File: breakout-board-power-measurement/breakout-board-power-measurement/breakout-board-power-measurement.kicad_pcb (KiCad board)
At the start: 2 copper layers, 62 parts, among them J1 Screw_Terminal_01x04, J2 Conn_01x07, J3 Conn_01x07, J4 Conn_01x02, Q1 NMOS, Q2 NMOS, U1 MCP3911A0-E-SS, U2 Si8641BA-B-IU, U3 LM317_3PinPackage, U4 LM2575-3.3BT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

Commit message: Important updates and fine tunings to schematic
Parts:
- removed D1, D2: 3.6, Diode_SMD:D_1206_3216Metric
- removed PS1: ITQ4803SA-H, Converter_DCDC:Converter_DCDC_XP_POWER-ITQxxxxS-H_THT
- removed Q1, Q2: NMOS, Package_TO_SOT_SMD:TO-252-2
- removed U4: LM2575-3.3BT, Package_TO_SOT_THT:TO-220-5_Vertical
- added PS2: IA0505S, Converter_DCDC:Converter_DCDC_XP_POWER-IAxxxxS_THT, F.Cu at (154.1, 90.9)
- J2: value Conn_01x07 -> Conn_01x09; footprint Connector_PinSocket_2.54mm:PinSocket_1x07_P2.54mm_Vertical -> Connector_PinSocket_2.54mm:PinSocket_1x09_P2.54mm_Vertical
- R10, R11: value 10k -> 180k
- R6, R7: value 270k -> 150k
- R8: value 100k -> 10k
- R9: value 10E -> 50m
- U2: footprint Package_SO:QSOP-16_3.9x4.9mm_P0.635mm -> Package_SO:SOIC-16_3.9x9.9mm_P1.27mm
- U3: value LM317_3PinPackage -> LM317_TO-252; footprint Package_TO_SOT_SMD:SOT-89-3_Handsoldering -> Package_TO_SOT_SMD:TO-252-2
- moved U3 59.0 mm to (169.9, 111.4)
- moved R10 39.2 mm to (167.0, 82.0), turned to 0 degrees
- moved R11 36.6 mm to (167.0, 85.3)
- moved C10 11.6 mm to (176.5, 121.8)
- moved C9 11.6 mm to (160.7, 121.8)
- moved FB1 11.6 mm to (168.5, 121.8)
- moved R13 11.6 mm to (167.1, 126.9)
- moved R14 11.6 mm to (170.4, 126.9)
- moved C11 1.98 mm to (205.1, 134.8)
- moved C12 1.98 mm to (205.1, 138.2)
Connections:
- R10 pad 1: Net-(D1-A) -> Net-(R10-Pad1)
- R10 pad 2: GNDA -> Net-(R10-Pad2)
- R11 pad 1: Net-(D2-A) -> Net-(R10-Pad2)
- R11 pad 2: GNDD -> Net-(R11-Pad2)
- R7 pad 2: Net-(R7-Pad2) -> Net-(R10-Pad1)
- R8 pad 1: Net-(R7-Pad2) -> Net-(R11-Pad2)
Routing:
- net Net-(R7-Pad2): track 27.8 -> 0.00 mm
- net (no net): track 0.00 -> 27.8 mm

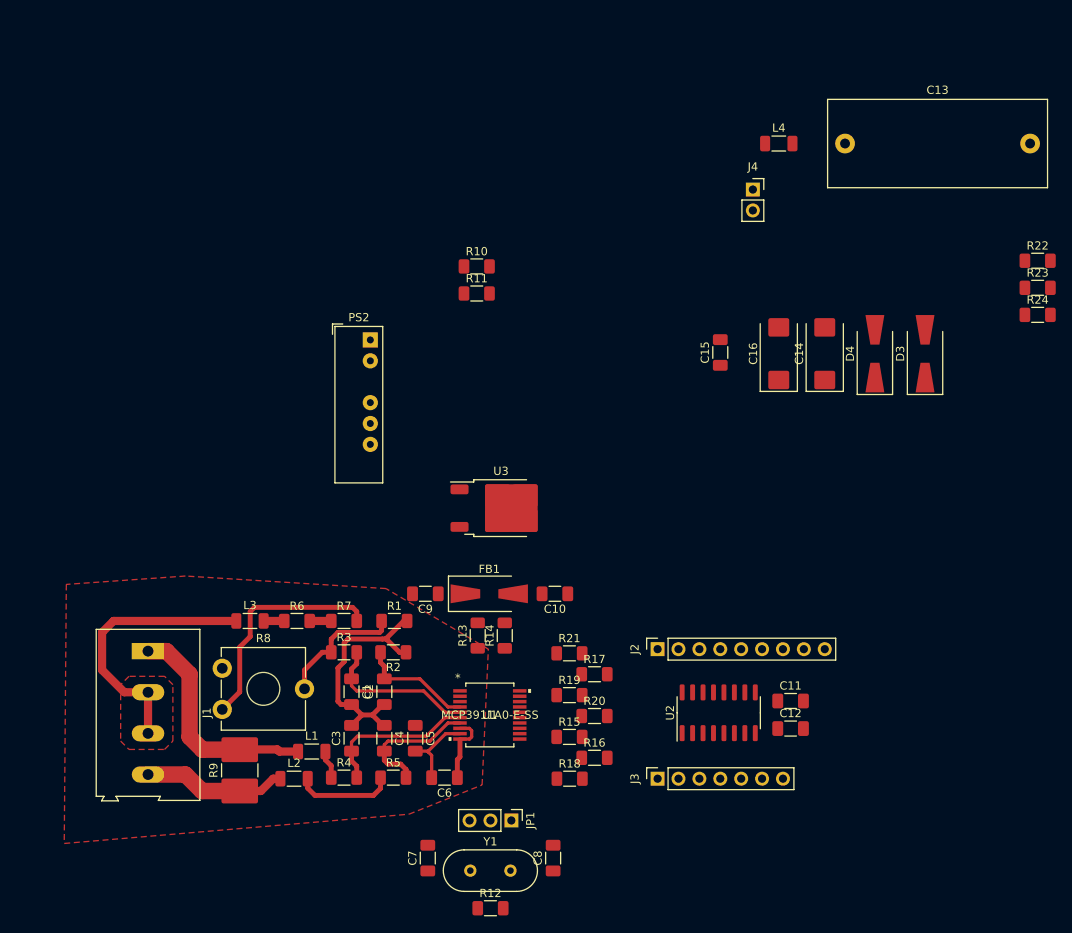
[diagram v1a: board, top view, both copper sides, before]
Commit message: Power measurement PCB 95% Done. Whats missing: proper cooil footprints, capacitive power supply net
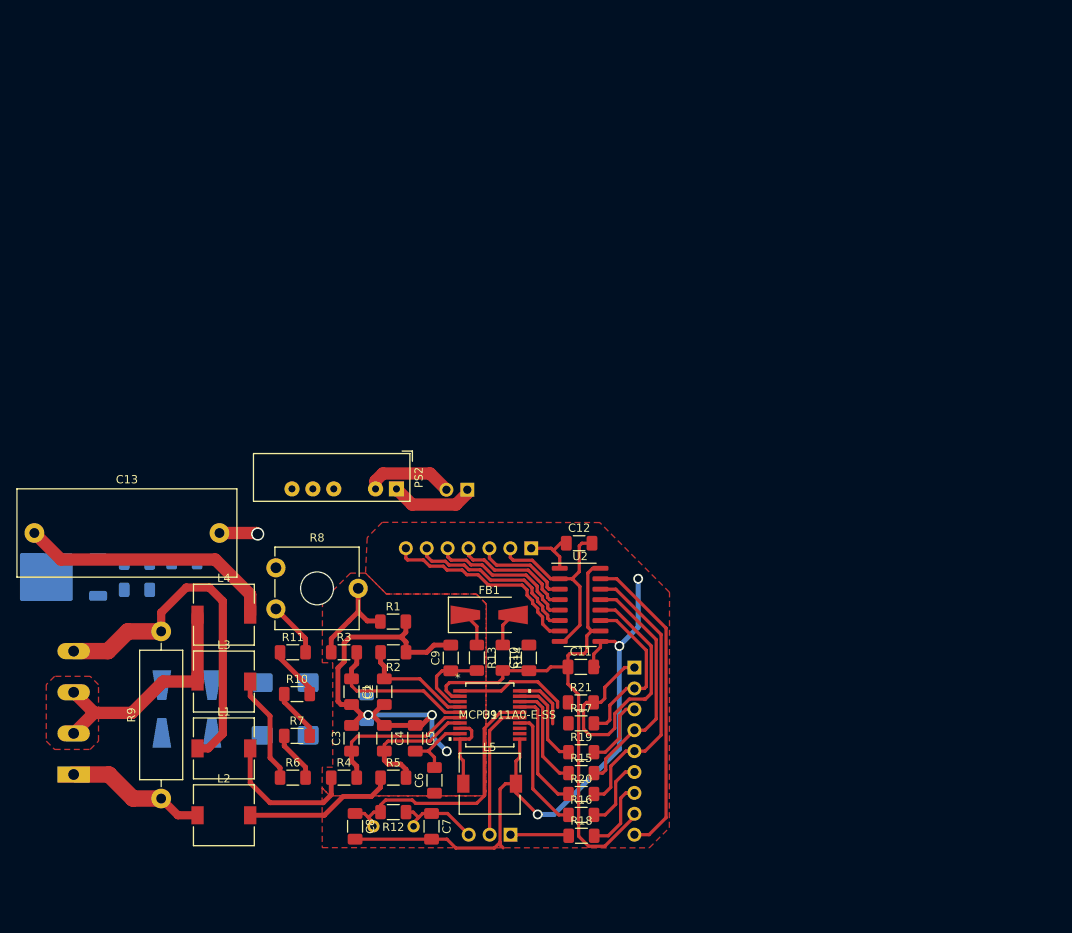
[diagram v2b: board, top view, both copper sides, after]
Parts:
- added L5: 150n/300m, Inductor_SMD:L_7.3x7.3_H4.5, F.Cu at (168.6, 144.9)
- C14, C15, C16, D3, D4, J1, J2, J3, J4, JP1, R22, R23, R24, U3, Y1: moved to B.Cu
- L1, L2, L3, L4: footprint Inductor_SMD:L_1206_3216Metric_Pad1.22x1.90mm_HandSolder -> Inductor_SMD:L_7.3x7.3_H4.5
- R9: footprint Resistor_SMD:R_2816_7142Metric -> Resistor_THT:R_Axial_DIN0516_L15.5mm_D5.0mm_P20.32mm_Horizontal
- moved R23 114.5 mm to (125.7, 118.0), turned to 180 degrees
- moved R24 114.5 mm to (125.7, 121.3), turned to 180 degrees
- moved R22 110.0 mm to (131.4, 118.0), turned to 180 degrees
- moved C13 109.3 mm to (113.2, 114.4)
- moved D3 102.3 mm to (128.7, 135.8)
- moved D4 91.4 mm to (134.8, 135.8)
- moved L4 88.5 mm to (136.2, 124.3)
- moved C14 80.9 mm to (140.9, 135.8)
- moved C16 71.7 mm to (146.5, 135.8)
- moved C15 60.9 mm to (153.6, 135.6)
- moved R10 56.4 mm to (145.1, 134.0)
- moved U3 54.7 mm to (115.9, 119.8), turned to 180 degrees
- moved J4 50.4 mm to (165.8, 109.1), turned to 90 degrees
- moved R11 49.0 mm to (144.6, 128.9)
- moved C12 34.2 mm to (179.4, 115.6)
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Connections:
- C12 pad 2: Net-(J3-Pin_7) -> Net-(J3-Pin_2)
- J1 pad 1: /current_pos -> /current_neg
- J1 pad 2: /HIGH_in -> HIGH_in
- J1 pad 3: /HIGH_in -> HIGH_in
- J1 pad 4: /current_neg -> /current_pos
- L3 pad 1: /HIGH_in -> HIGH_in
- L4 pad 1: HIGH -> HIGH_in
- R15 pad 2: Net-(J2-Pin_3) -> Net-(J2-Pin_4)
- R18 pad 2: Net-(J2-Pin_5) -> Net-(J2-Pin_7)
- R19 pad 2: Net-(J2-Pin_1) -> Net-(J2-Pin_3)
- R20 pad 2: Net-(J2-Pin_4) -> Net-(J2-Pin_5)
- R21 pad 2: Net-(J2-Pin_7) -> Net-(J2-Pin_1)
- U2 pad 13: Net-(J2-Pin_3) -> Net-(J2-Pin_4)
- U2 pad 14: Net-(J2-Pin_4) -> Net-(J2-Pin_5)
- U2 pad 2: Net-(J3-Pin_7) -> Net-(J3-Pin_2)
- U2 pad 7: Net-(J3-Pin_2) -> Net-(J3-Pin_7)
- U2 pad 8: Net-(J3-Pin_7) -> Net-(J3-Pin_2)
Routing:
- net GNDD: track 0.00 -> 117.9 mm, vias 0 -> 3
- net /3V3D: track 0.00 -> 65.8 mm
- net Net-(J2-Pin_1): track 0.00 -> 37.2 mm
- net Net-(J2-Pin_5): track 0.00 -> 34.5 mm
- net /HIGH_in: track 33.2 -> 0.00 mm
- net /OSC2: track 0.00 -> 32.5 mm
- net Net-(C13-Pad1): track 0.00 -> 31.8 mm
- net Net-(J2-Pin_4): track 0.00 -> 29.5 mm
- net HIGH_in: track 0.00 -> 29.3 mm
- net (no net): track 27.8 -> 0.00 mm
- net GNDA: track 38.5 -> 64.0 mm, vias 0 -> 3
- net Net-(J3-Pin_2): track 0.00 -> 25.0 mm
- net Net-(J3-Pin_7): track 0.00 -> 24.9 mm
- net Net-(J3-Pin_6): track 0.00 -> 21.4 mm
- net Net-(J2-Pin_2): track 0.00 -> 20.7 mm
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- added copper zone on F.Cu, net GNDD
- added copper zone on F.Cu, net HIGH_in
- removed copper zone on F.Cu, net /HIGH_in
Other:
- board text added: "C8"
